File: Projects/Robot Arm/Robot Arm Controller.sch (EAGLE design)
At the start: 70 parts, among them IC1 U_FTDICHIP_FT232RL, J1 ICSP HEADER, J2 SERVO PWR, J3 STEPPER, J4 J_MOLEX_502386, P1 P_USB_MINIUX60A-MB-5ST, P2 +12V INPUT, Q1 STN2NF10, U1 UA78M05CDCY, U2 TPS71550DCKR, U3 U_ATMEGA328P-AU, U4 U_5VSWITCHER_LM2576SX-5.0, U5 A4988ALT1, U6 U_OPAMP_MCP6001T-E/OT, Y1 CSTCE16M0V13

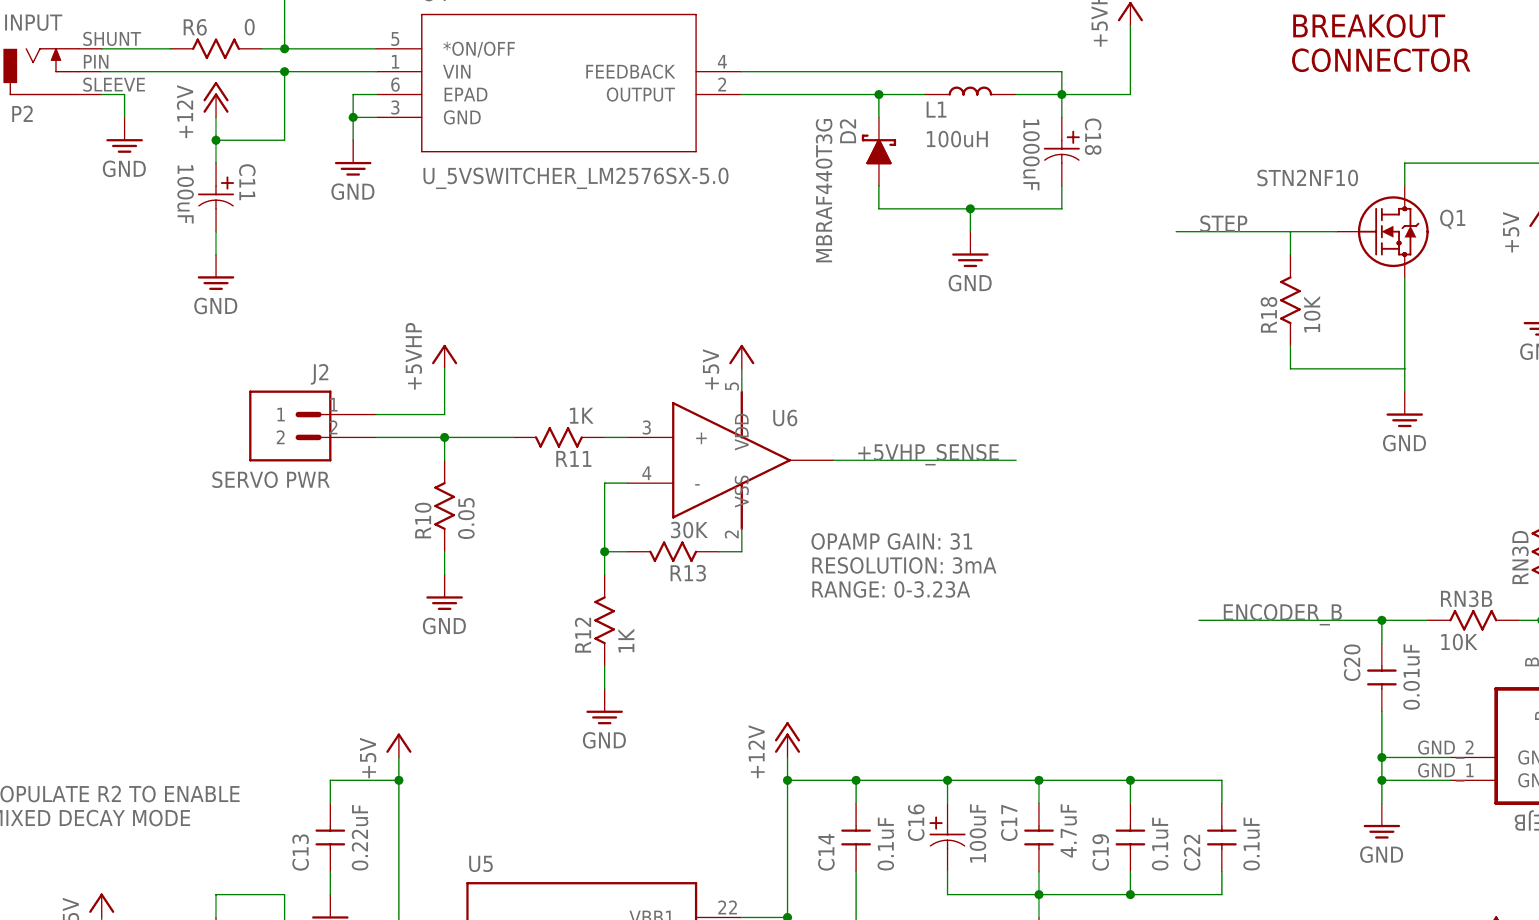
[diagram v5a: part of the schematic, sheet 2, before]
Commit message: FTDI and motor controller routed
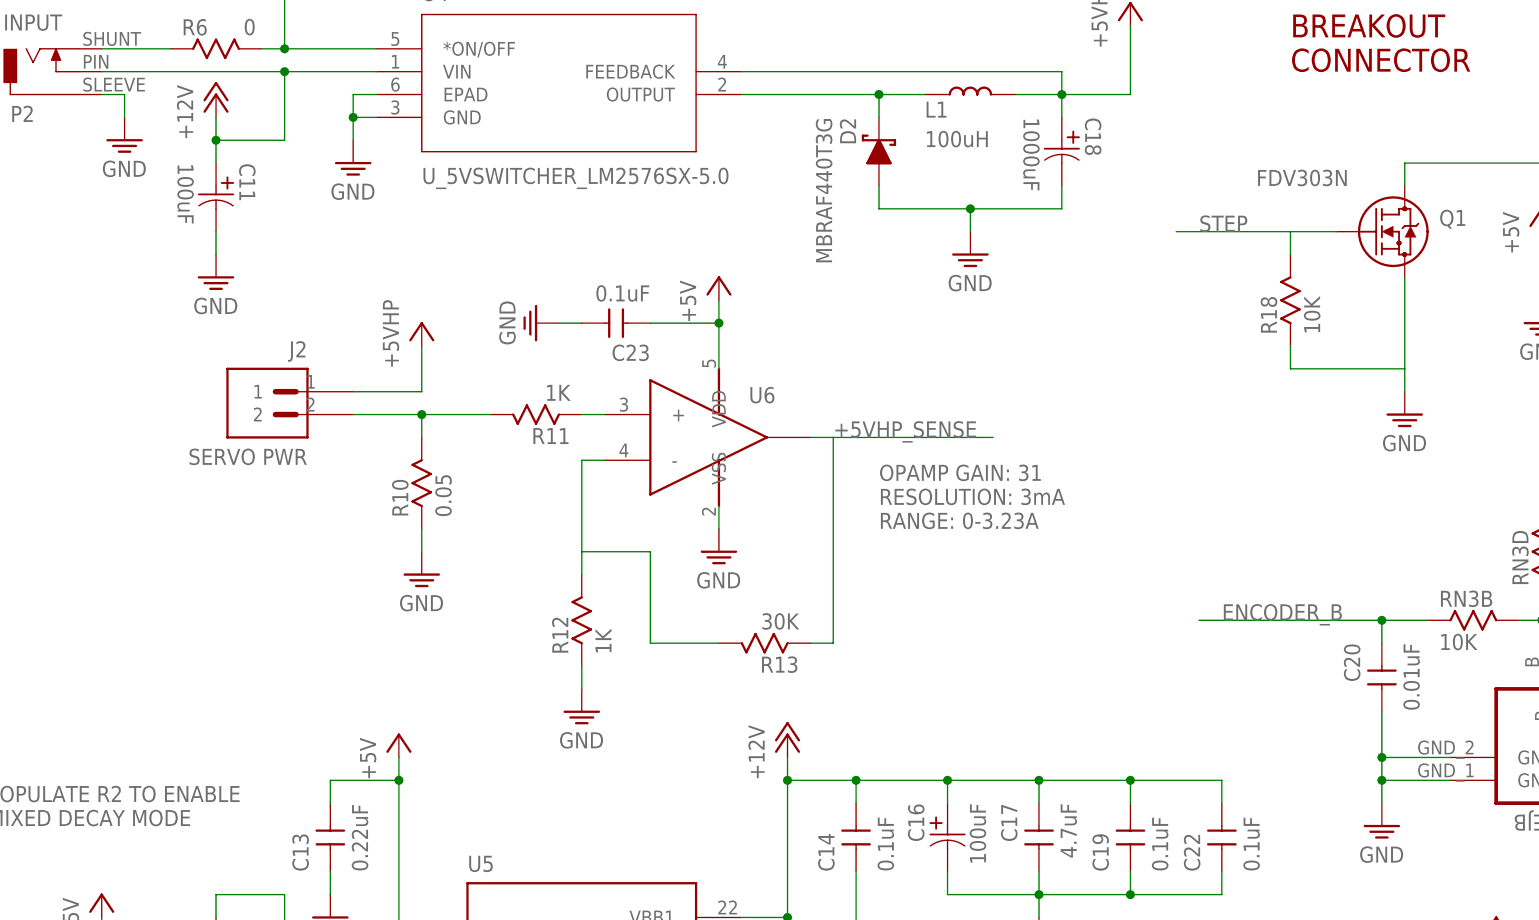
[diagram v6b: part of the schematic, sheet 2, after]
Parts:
- added C23: 0.1uF, devon:C_CAPACITORC0805
- C17: device devon:C_CAPACITORC1206 -> devon:C_CAPACITORC0805
- Q1: value STN2NF10 -> FDV303N; device devon:Q_MOSFET_STN2NF10 -> devon:Q_MOSFET_FDV303N
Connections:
- removed net N$42: R13.1, U6.VSS
- new net +5VHP: C18.+, J2.1, L1.2, U4.FEEDBACK
- new net VUSB: C3.1, C5.1, D1.A, P1.5
- net +5V: now also C23.2, RN1B.1; no longer C18.+, C3.1, C5.1, D1.A, J2.1, L1.2, P1.5, RN1B.2, U4.FEEDBACK
- net +5VHP_SENSE: now also R13.1
- net BASE_LED: now also Q1.DRAIN; no longer Q1.2
- net GND: now also C23.1, Q1.SOURCE, U6.VSS; no longer Q1.3
- net N$17: now also LED1.A, RN1B.2; no longer LED2.A, RN1A.1
- net N$3: now also LED2.A, RN1A.2; no longer LED1.A, RN1B.1
- net STAT: now also RN1A.1; no longer RN1A.2
- net STEP: now also Q1.GATE; no longer Q1.1
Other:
- moved on the sheet: J2, R10, R11, R12, R13, RN1B, RN2A, U6

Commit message: Almost done
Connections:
- net +5V: now also RN2C.2; no longer RN2A.2
- net N$9: now also RN2A.1; no longer RN2C.1
- net RESET: now also RN2C.1; no longer RN2A.1
- net TX: now also RN2A.2; no longer RN2C.2
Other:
- moved on the sheet: RN2A, RN2C
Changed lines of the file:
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@@
 <instance part="C10" gate="G$1" x="124.46" y="-30.48" rot="R90"/>
 <instance part="C7" gate="G$1" x="114.3" y="-30.48" rot="R90"/>
-<instance part="RN2" gate="A" x="213.36" y="-35.56" rot="R90"/>
+<instance part="RN2" gate="A" x="226.06" y="-68.58"/>
 <instance part="RN2" gate="B" x="226.06" y="-60.96"/>
-<instance part="RN2" gate="C" x="226.06" y="-68.58"/>
+<instance part="RN2" gate="C" x="213.36" y="-35.56" rot="R90"/>
 <instance part="RN2" gate="D" x="195.58" y="-142.24"/>
 <instance part="LED2" gate="G$1" x="86.36" y="-71.12" rot="R270"/>
@@
 <segment>
 <pinref part="U3" gate="A" pin="PC6(RESET)"/>
-<pinref part="RN2" gate="A" pin="1"/>
 <wire x1="185.42" y1="-45.72" x2="213.36" y2="-45.72" width="0.1524" layer="91"/>
 <wire x1="213.36" y1="-45.72" x2="213.36" y2="-43.18" width="0.1524" layer="91"/>
 <label x="187.96" y="-45.72" size="1.778" layer="95"/>
 <pinref part="S1" gate="G$1" pin="1"/>
-<wire x1="213.36" y1="-43.18" x2="213.36" y2="-40.64" width="0.1524" layer="91"/>
 <wire x1="215.9" y1="-43.18" x2="213.36" y2="-43.18" width="0.1524" layer="91"/>
 <wire x1="213.36" y1="-45.72" x2="213.36" y2="-48.26" width="0.1524" layer="91"/>
@@
 <wire x1="213.36" y1="-48.26" x2="215.9" y2="-48.26" width="0.1524" layer="91"/>
 <junction x="213.36" y="-45.72"/>
-<junction x="213.36" y="-43.18"/>
+<pinref part="RN2" gate="C" pin="1"/>
+<wire x1="213.36" y1="-40.64" x2="213.36" y2="-43.18" width="0.1524" layer="91"/>
 </segment>
 <segment>
@@
 </net>
 <net name="+5V" class="0">
-<segment>
-<pinref part="RN2" gate="A" pin="2"/>
-<wire x1="213.36" y1="-30.48" x2="213.36" y2="-27.94" width="0.1524" layer="91"/>
-<pinref part="P+11" gate="1" pin="+5V"/>
-</segment>
 <segment>
 <pinref part="U1" gate="A" pin="VOUT"/>
@@
 <junction x="114.3" y="-20.32"/>
 </segment>
+<segment>
+<pinref part="P+11" gate="1" pin="+5V"/>
+<pinref part="RN2" gate="C" pin="2"/>
+<wire x1="213.36" y1="-27.94" x2="213.36" y2="-30.48" width="0.1524" layer="91"/>
+</segment>
 </net>
 <net name="ENCODER_A" class="0">
@@
 <wire x1="185.42" y1="-53.34" x2="213.36" y2="-53.34" width="0.1524" layer="91"/>
 <wire x1="213.36" y1="-53.34" x2="213.36" y2="-68.58" width="0.1524" layer="91"/>
+<pinref part="RN2" gate="A" pin="1"/>
 <wire x1="213.36" y1="-68.58" x2="220.98" y2="-68.58" width="0.1524" layer="91"/>
-<pinref part="RN2" gate="C" pin="1"/>
 </segment>
 </net>
@@
 <net name="TX" class="0">
 <segment>
-<pinref part="RN2" gate="C" pin="2"/>
-<wire x1="231.14" y1="-68.58" x2="238.76" y2="-68.58" width="0.1524" layer="91"/>
-<label x="233.68" y="-68.58" size="1.778" layer="95"/>
-</segment>
-<segment>
 <pinref part="IC1" gate="1" pin="RXD"/>
 <wire x1="101.6" y1="-114.3" x2="137.16" y2="-114.3" width="0.1524" layer="91"/>
 <label x="124.46" y="-114.3" size="1.778" layer="95"/>
 </segment>
-</net>
+<segment>
+<pinref part="RN2" gate="A" pin="2"/>
+<wire x1="231.14" y1="-68.58" x2="238.76" y2="-68.58" width="0.1524" layer="91"/>
+<label x="233.68" y="-68.58" size="1.778" layer="95"/>
+</segment>
+</net>

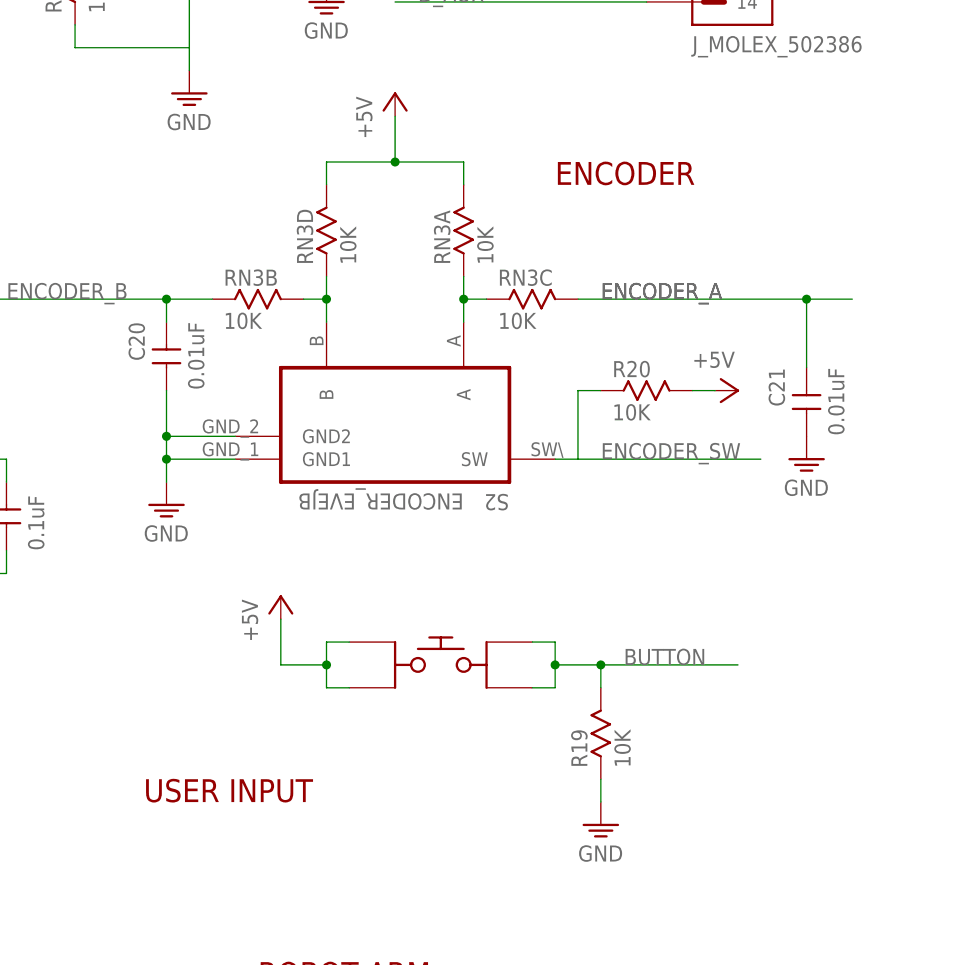
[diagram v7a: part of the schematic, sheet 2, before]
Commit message: everything done except ground planes
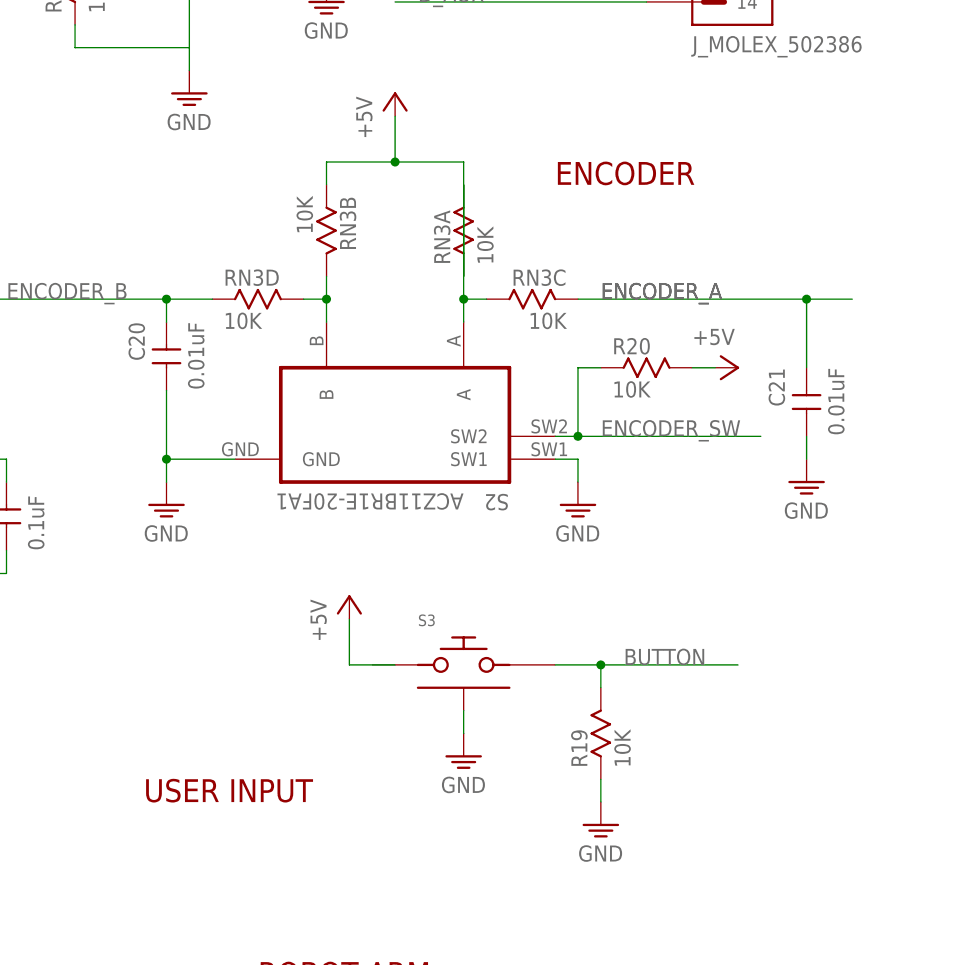
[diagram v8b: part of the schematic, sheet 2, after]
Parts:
- S2: value ENCODER_EVEJB -> ACZ11BR1E-20FA1; device devon:S_ENCODER_EVEJB -> devon:S_ENCODER_ACZ11BR1E-20FA1-20C
- S3: value S_BUTTON_TACTILE_PTS645 -> S_BUTTON_TACTILE_KT11S1SA2M35LFG; device devon:S_BUTTON_TACTILE_PTS645 -> devon:S_BUTTON_TACTILE_KT11S1SA2M35LFG
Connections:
- removed net D11/MOSI: J1.4
- removed net D12/MISO: J1.1
- removed net D13/SCK: J1.3
- new net N$37: S1.2
- new net N$38: S1.4
- net +5V: now also RN3A.1, RN3B.1; no longer RN3A.2, RN3D.2, S3.1, S3.2
- net BUTTON: now also S3.2; no longer S3.3, S3.4
- net ENCODER_A: now also RN3C.1; no longer RN3C.2
- net ENCODER_B: now also RN3D.1; no longer RN3B.1
- net ENCODER_SW: now also S2.SW2; no longer S2.SW
- net GND: now also S1.1, S2.GND, S2.SW1, S3.HOUSING; no longer S1.3, S1.4, S2.GND1, S2.GND2
- net GRIP_LED: now also J1.1
- net GRIP_PWM: now also J1.4
- net N$34: now also RN3D.2; no longer RN3D.1
- net N$36: now also RN3A.2, RN3C.2; no longer RN3A.1, RN3C.1
- net RESET: now also S1.3; no longer S1.1, S1.2
- net STAT: now also J1.3
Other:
- moved on the sheet: R20, RN3B, RN3D, S2
